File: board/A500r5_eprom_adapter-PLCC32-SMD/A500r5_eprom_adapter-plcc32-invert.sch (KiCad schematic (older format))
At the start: 11 parts, among them J2 A18 Selector, J3 A19 Selector, U1 27C400-A500, U2 27C080-L, U3 27C080-L

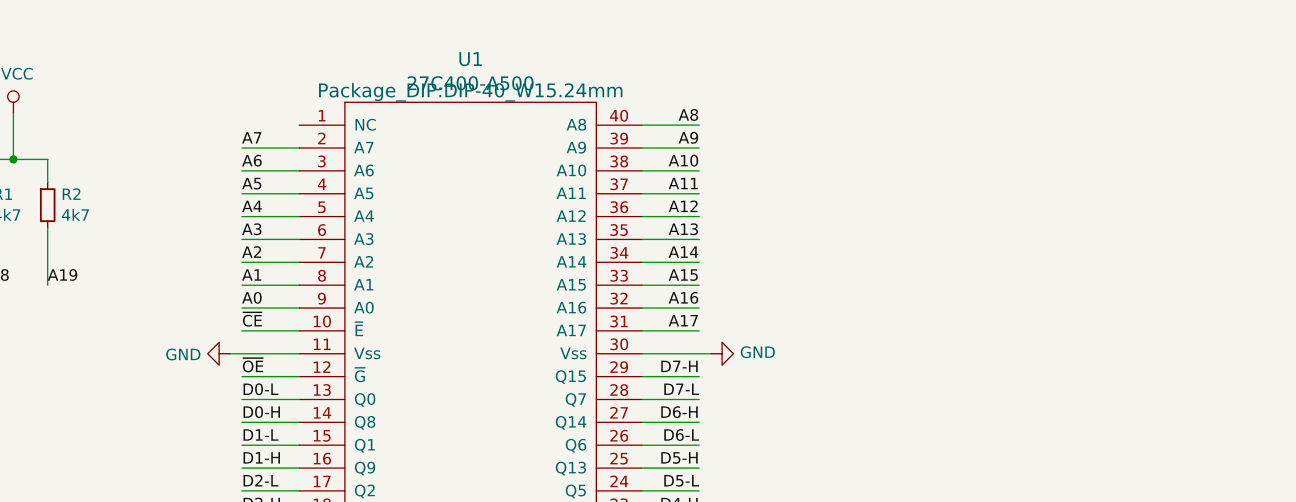
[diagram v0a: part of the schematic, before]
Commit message: Add A17 pin selector
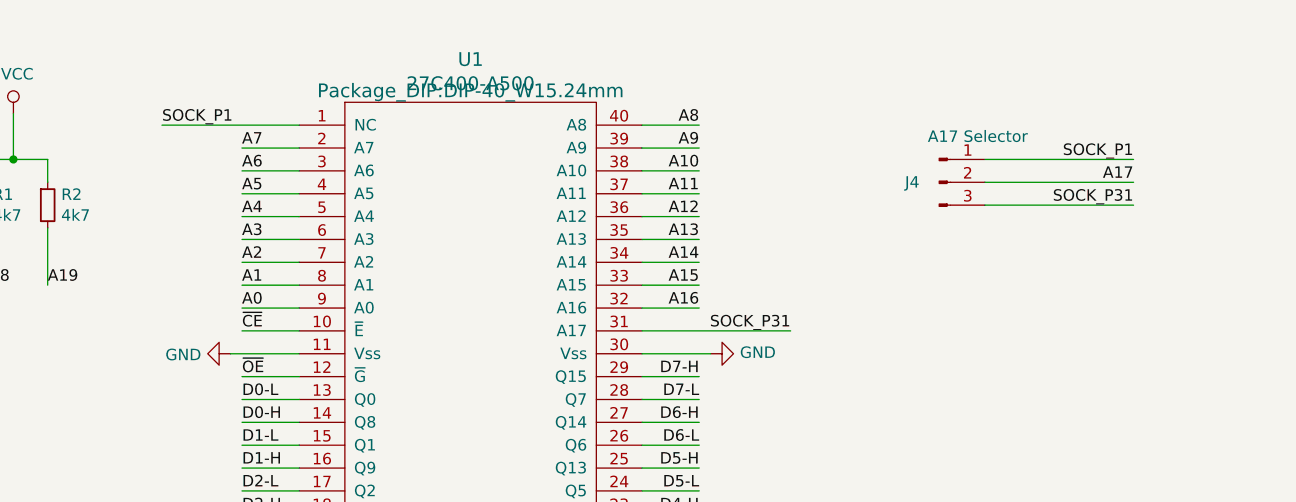
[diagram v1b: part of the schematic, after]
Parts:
- added J4: A17 Selector, Connector_PinHeader_2.54mm:PinHeader_1x03_P2.54mm_Vertical, symbol Connector:Conn_01x03_Male
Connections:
- net A17: now also J4.2 (Pin_2); no longer U1.31 (A17)
- net SOCK_P1: now reaches U1.1 (NC)
- net SOCK_P1: now also J4.1 (Pin_1)
- new net SOCK_P31: J4.3 (Pin_3), U1.31 (A17)
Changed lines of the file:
@@
 	5200 2000 4950 2000
-Wire Wire Line
-	5200 2100 4950 2100
 Wire Wire Line
 	3450 2100 3200 2100
@@
 Text Label 5200 2000 2    50   ~ 0
 A16
-Text Label 5200 2100 2    50   ~ 0
-A17
 Text Label 5200 3000 2    50   ~ 0
 D4-L
@@
 	2350 1350 2350 1450
 $Comp
-L power:VCC #PWR?
+L power:VCC #PWR0110
 U 1 1 5E5AE0F9
 P 2200 1150
-F 0 "#PWR?" H 2200 1000 50  0001 C CNN
+F 0 "#PWR0110" H 2200 1000 50  0001 C CNN
 F 1 "VCC" H 2217 1323 50  0000 C CNN
 F 2 "" H 2200 1150 50  0001 C CNN
@@
 Text Label 2350 1900 0    50   ~ 0
 A19
+$Comp
+L Connector:Conn_01x03_Male J4
+U 1 1 5F3C08B3
+P 6250 1450
+F 0 "J4" H 6100 1450 50  0000 L CNN
+F 1 "A17 Selector" H 6200 1650 50  0000 L CNN
+F 2 "Connector_PinHeader_2.54mm:PinHeader_1x03_P2.54mm_Vertical" H 6250 1450 50  0001 C CNN
+F 3 "~" H 6250 1450 50  0001 C CNN
+	1    6250 1450
+	1    0    0    -1
+$EndComp
+Wire Wire Line
+	6450 1450 7100 1450
+Text Label 7100 1450 2    50   ~ 0
+A17
+Wire Wire Line
+	6450 1350 7100 1350
+Text Label 7100 1350 2    50   ~ 0
+SOCK_P1
+Wire Wire Line
+	6450 1550 7100 1550
+Text Label 7100 1550 2    50   ~ 0
+SOCK_P31
+Wire Wire Line
+	4950 2100 5600 2100
+Text Label 5600 2100 2    50   ~ 0
+SOCK_P31
+Wire Wire Line
+	3450 1200 2850 1200
+Text Label 2850 1200 0    50   ~ 0
+SOCK_P1
 $EndSCHEMATC
